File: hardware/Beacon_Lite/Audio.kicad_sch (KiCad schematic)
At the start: 0 parts

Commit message: Started ST project. Create sch symbols.
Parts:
- added U1: OPA1678ID, symbol Beacon_Lite_Library:OPA1678ID
- added U7: XS3A4051, symbol Beacon_Lite_Library:XS3A4051
- added U8: TLV320AIC3104, symbol Beacon_Lite_Library:TLV320AIC3104

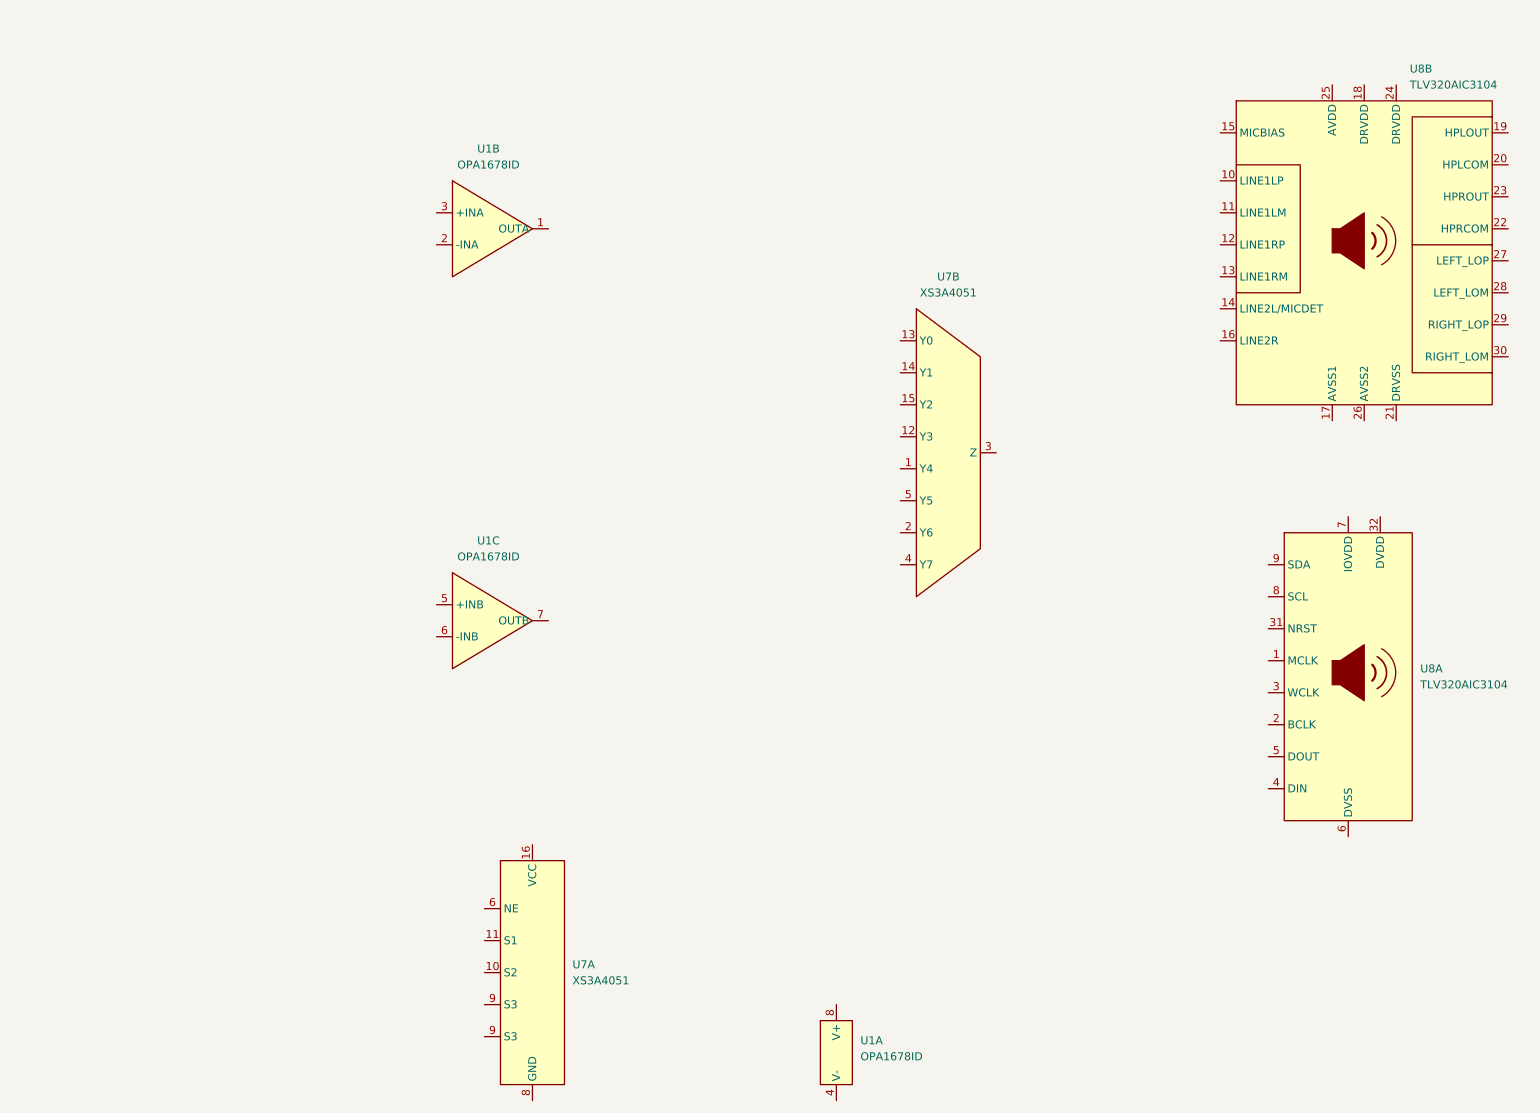
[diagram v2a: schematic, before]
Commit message: Started programming NUCLEO-H533 in VSCODE
* Able to use C++ and C
* Successful able to debug
* Can blink an LED when button is pressed via an interrupt.
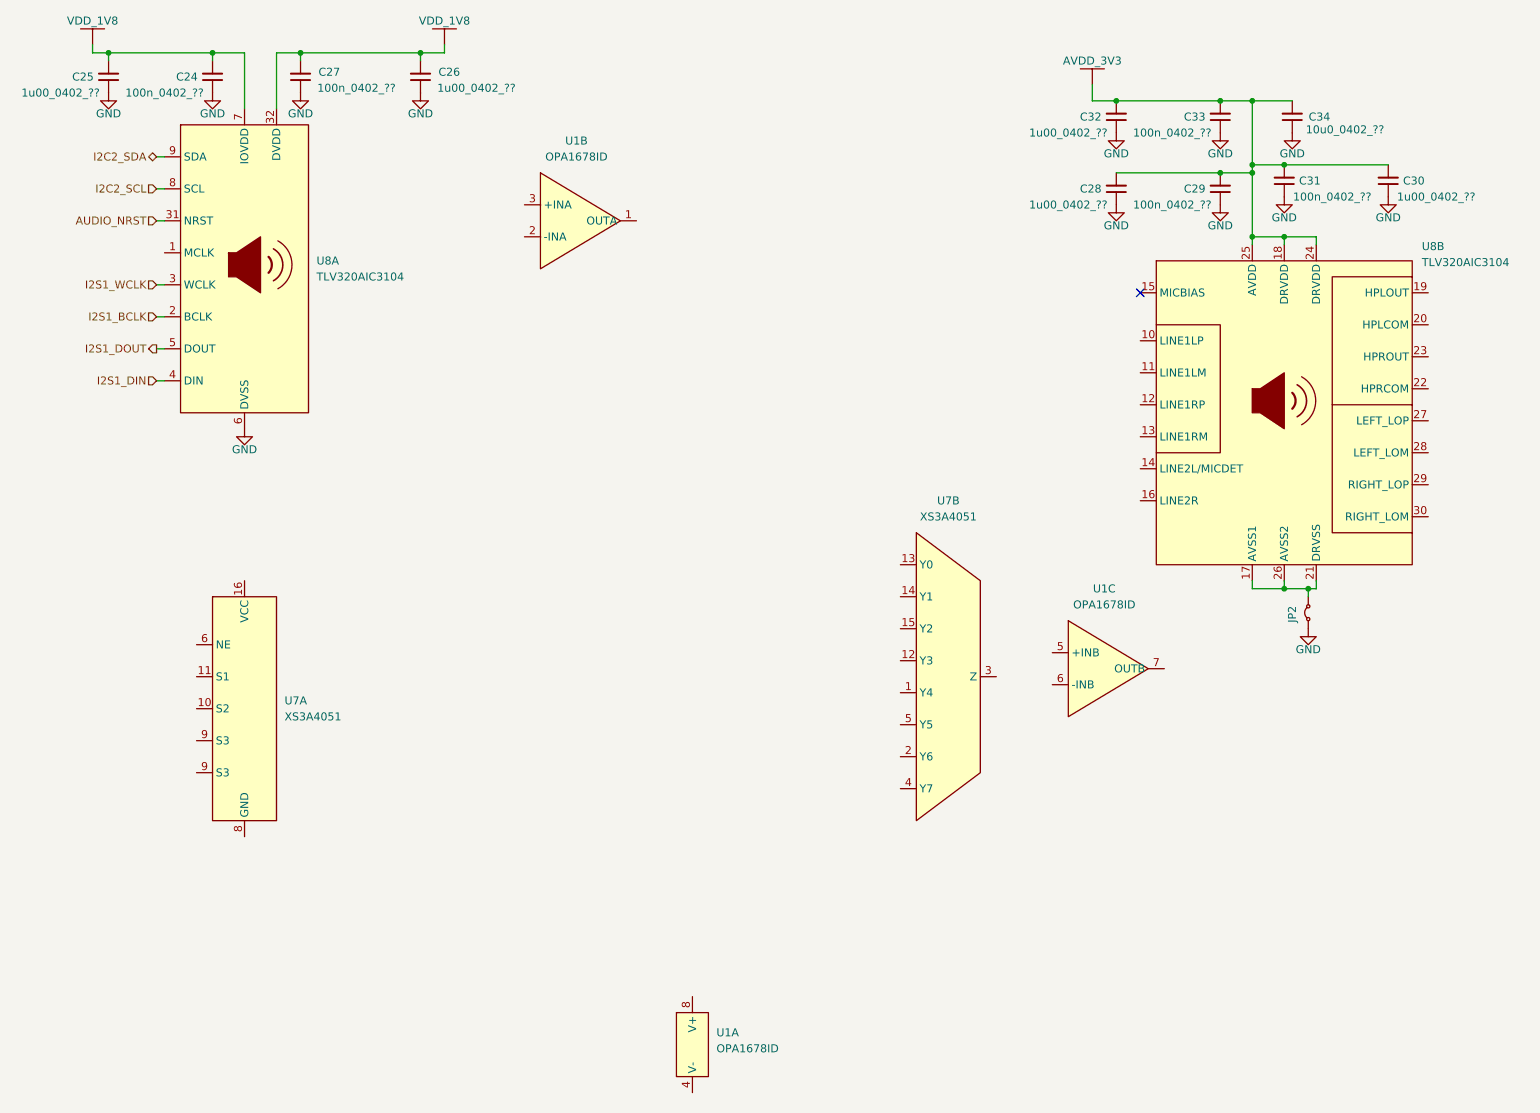
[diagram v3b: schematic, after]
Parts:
- added C24, C27, C29, C31, C33: 100n_0402_??, Footprint_Library:0402_1005Metric_Handsolder, symbol Device:C_Small
- added C25, C26, C28, C30, C32: 1u00_0402_??, Footprint_Library:0402_1005Metric_Handsolder, symbol Device:C_Small
- added C34: 10u0_0402_??, Footprint_Library:0402_1005Metric_Handsolder, symbol Device:C_Small
- added JP2: Jumper_2_Small_Bridged, symbol Jumper:Jumper_2_Small_Bridged
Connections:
- net I2S1_BCLK: now reaches U8.2 (BCLK)
- net I2S1_WCLK: now reaches U8.3 (WCLK)
- net AUDIO_NRST: now reaches U8.31 (NRST)
- net VDD_1V8: now reaches U8.32 (DVDD)
- net VDD_1V8: now also U8.7 (IOVDD), C24.2, C25.2, C26.2, C27.2
- net I2S1_DIN: now reaches U8.4 (DIN)
- net I2S1_DOUT: now reaches U8.5 (DOUT)
- net GND: now reaches U8.6 (DVSS)
- net GND: now also C24.1, C25.1, C26.1, C27.1, C28.1, C29.1, C30.1, C31.1, C32.1, C33.1, C34.1, JP2.1 (A)
- net I2C2_SCL: now reaches U8.8 (SCL)
- net I2C2_SDA: now reaches U8.9 (SDA)
- net at U8.17 (AVSS1): now also U8.21 (DRVSS), U8.26 (AVSS2), JP2.2 (B)
- net AVDD_3V3: now reaches U8.18 (DRVDD)
- net AVDD_3V3: now also U8.24 (DRVDD), U8.25 (AVDD), C28.2, C29.2, C30.2, C31.2, C32.2, C33.2, C34.2
- no-connect marks 0 -> 1
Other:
- moved on the sheet: U1A, U1B, U1C, U7A, U7B, U8A, U8B
